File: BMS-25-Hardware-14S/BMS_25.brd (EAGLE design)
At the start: 139.7 x 52.1 mm, 218 parts, among them IC1 PBQ79656PAPTQ1, IC2 PBQ79656PAPTQ1, T1 PBHV8115X, 115, T2 PBHV8115X, 115

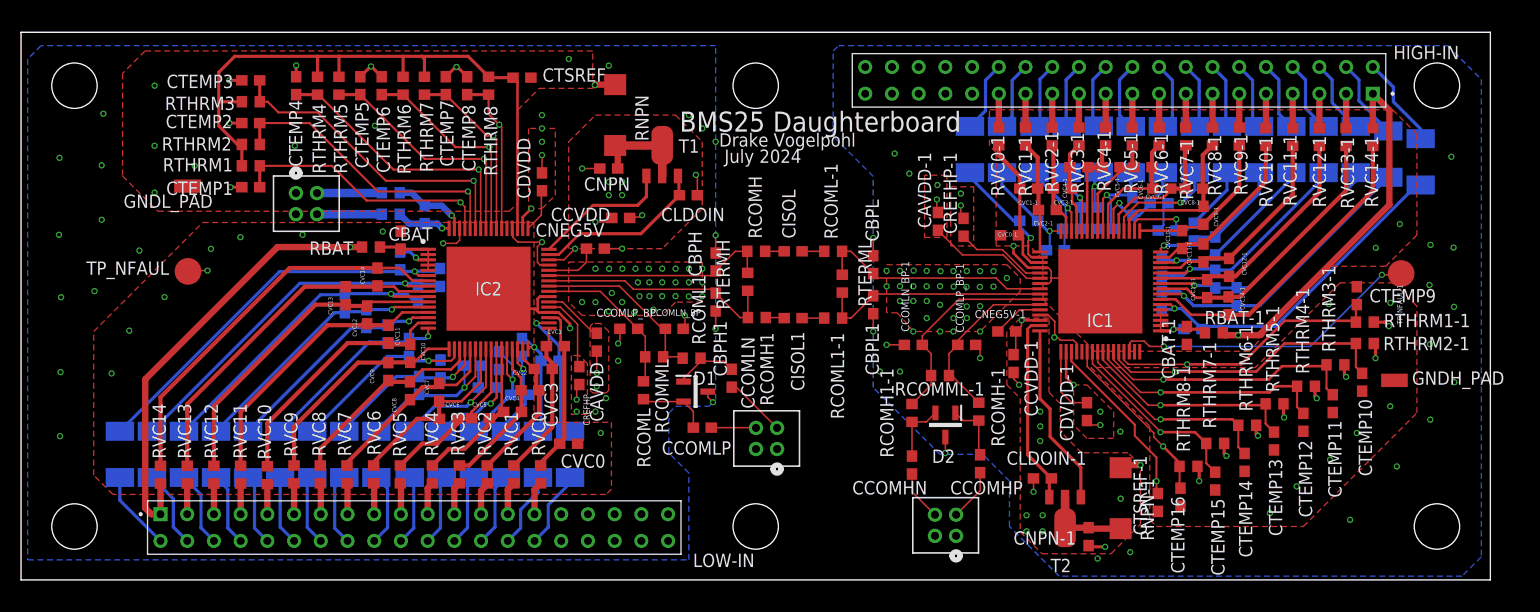
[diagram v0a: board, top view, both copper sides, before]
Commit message: Fixed Ground wiring
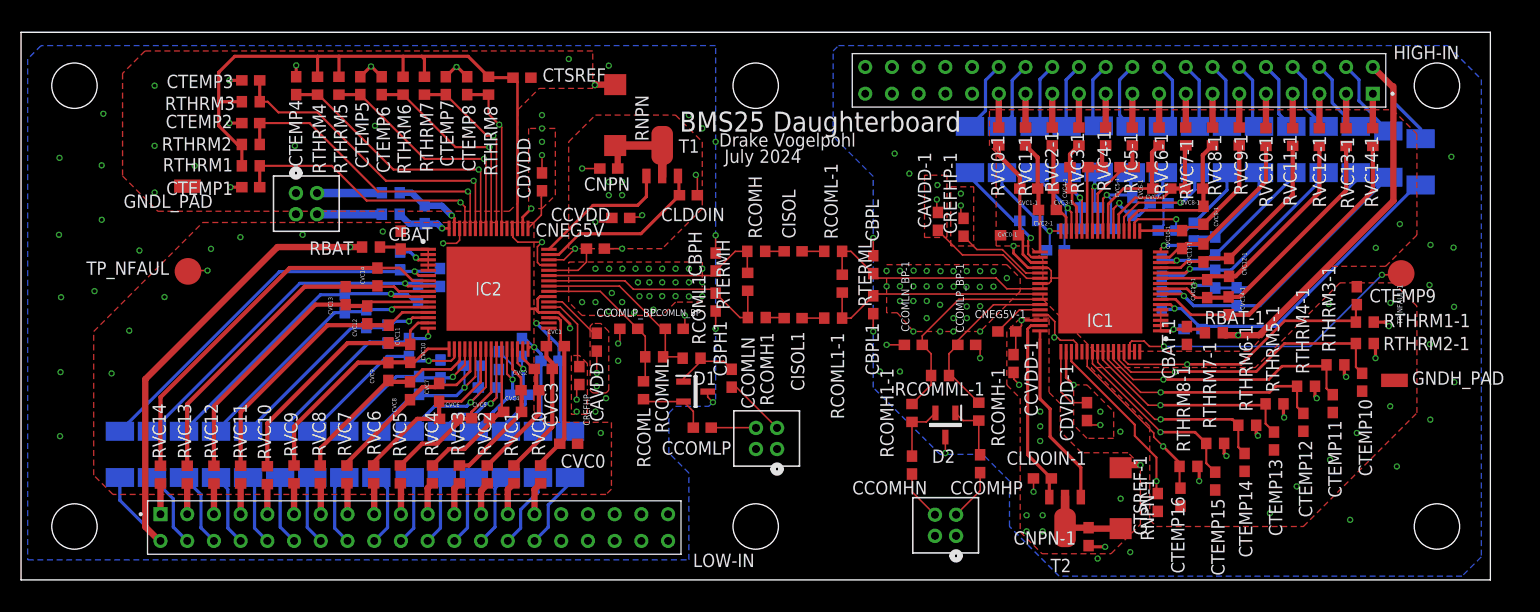
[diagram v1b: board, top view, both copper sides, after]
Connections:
- removed net CB14-IN: LOW-IN.02, RCB14.1
- removed net CB14-IN-1: HIGH-IN.02, RCB14-1.1
- new net VC14-IN: LOW-IN.01, RVC14.1
- new net VC14-IN-1: HIGH-IN.01, RVC14-1.1
- net BAT: now also LOW-IN.02, RCB14.1; no longer LOW-IN.01, RVC14.1
- net BAT-1: now also HIGH-IN.02, RCB14-1.1; no longer HIGH-IN.01, RVC14-1.1
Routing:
- net CB14-IN-1: track 8.73 -> 0.00 mm
- net BAT-1: track 55.5 -> 63.9 mm
- net CB14-IN: track 7.63 -> 0.00 mm
- net BAT: track 74.3 -> 81.1 mm
- net VC14-IN-1: track 0.00 -> 3.26 mm
- net VC14-IN: track 0.00 -> 2.91 mm

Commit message: Changed Connectors, pass DRC
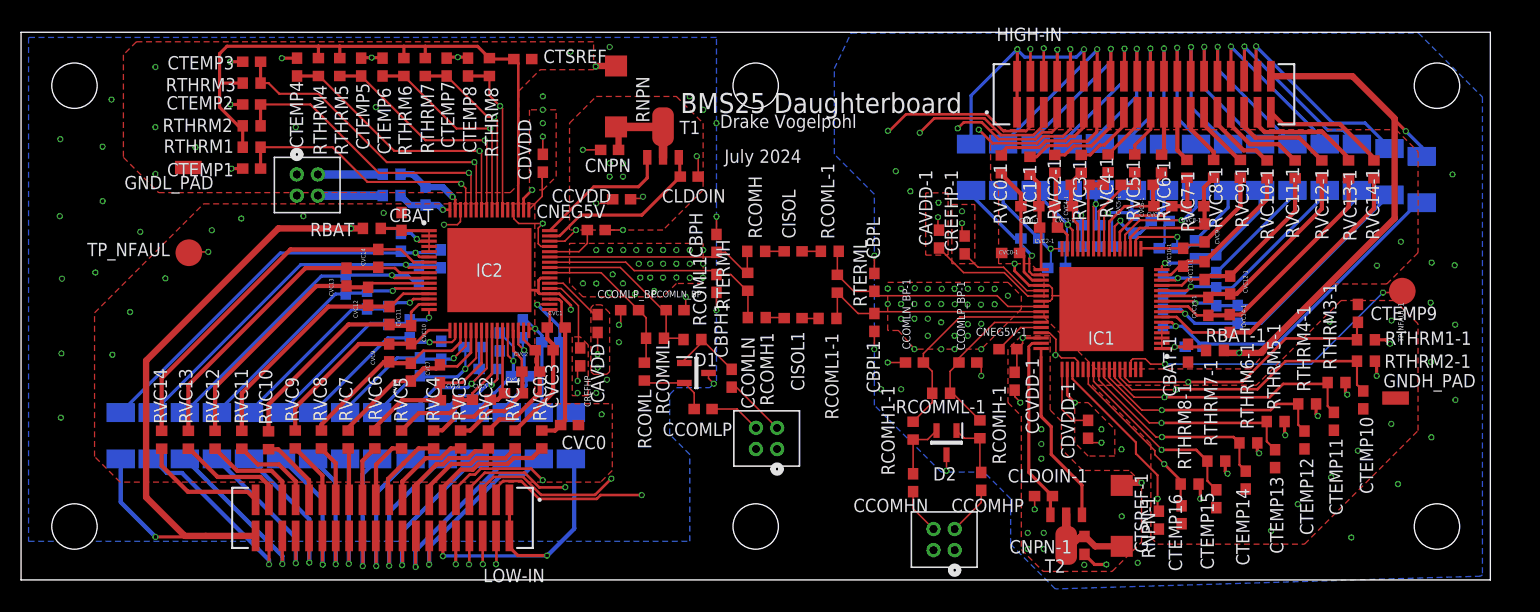
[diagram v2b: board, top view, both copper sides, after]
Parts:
- HIGH-IN, LOW-IN: value 87606-320LF -> TFM-120-02-L-D; device 87606-320LF:AMPHENOL_87606-320LF -> TFM-120-02-L-D:SAMTEC_TFM-120-02-L-D
- moved RVC10 3.32 mm to (23.5, 13.3)
- moved RVC0 3.32 mm to (49.5, 13.4)
- moved RVC1 3.32 mm to (47.0, 13.4)
- moved RVC11 3.32 mm to (21.0, 13.3)
- moved RVC12 3.32 mm to (18.5, 13.3)
- moved RVC13 3.32 mm to (15.9, 13.3)
- moved RVC14 3.32 mm to (13.4, 13.3)
- moved RVC2 3.32 mm to (44.4, 13.4)
- moved RVC3 3.32 mm to (41.8, 13.4)
- moved RVC4 3.32 mm to (39.2, 13.4)
- moved RVC5 3.32 mm to (36.2, 13.4)
- moved RVC6 3.32 mm to (33.6, 13.4)
- moved RVC7 3.32 mm to (31.1, 13.4)
- moved RVC8 3.32 mm to (28.6, 13.4)
- moved RVC9 3.32 mm to (26.1, 13.4)
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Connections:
- removed net CB0-IN: LOW-IN.30, RCB0.1
- removed net CB0-IN-1: HIGH-IN.30, RCB0-1.1
- new net VC0-IN: LOW-IN.11, RVC0.1
- new net VC0-IN-1: HIGH-IN.11, RVC0-1.1
- net BAT: now also LOW-IN.40; no longer LOW-IN.02
- net BAT-1: now also HIGH-IN.40; no longer HIGH-IN.02
- net CB1-IN: now also LOW-IN.14; no longer LOW-IN.28
- net CB1-IN-1: now also HIGH-IN.14; no longer HIGH-IN.28
- net CB10-IN: now also LOW-IN.32; no longer LOW-IN.10
- net CB10-IN-1: now also HIGH-IN.32; no longer HIGH-IN.10
- net CB11-IN: now also LOW-IN.34; no longer LOW-IN.08
- net CB11-IN-1: now also HIGH-IN.34; no longer HIGH-IN.08
- net CB12-IN: now also LOW-IN.36; no longer LOW-IN.06
- net CB12-IN-1: now also HIGH-IN.36; no longer HIGH-IN.06
- net CB13-IN: now also LOW-IN.38; no longer LOW-IN.04
- net CB13-IN-1: now also HIGH-IN.38; no longer HIGH-IN.04
- net CB2-IN: now also LOW-IN.16; no longer LOW-IN.26
- net CB2-IN-1: now also HIGH-IN.16; no longer HIGH-IN.26
- net CB3-IN: now also LOW-IN.18; no longer LOW-IN.24
- net CB3-IN-1: now also HIGH-IN.18; no longer HIGH-IN.24
- net CB4-IN: now also LOW-IN.20; no longer LOW-IN.22
- net CB4-IN-1: now also HIGH-IN.20; no longer HIGH-IN.22
- net CB5-IN: now also LOW-IN.22; no longer LOW-IN.20
- net CB5-IN-1: now also HIGH-IN.22; no longer HIGH-IN.20
- net CB6-IN: now also LOW-IN.24; no longer LOW-IN.18
- net CB6-IN-1: now also HIGH-IN.24; no longer HIGH-IN.18
- net CB7-IN: now also LOW-IN.26; no longer LOW-IN.16
- net CB7-IN-1: now also HIGH-IN.26; no longer HIGH-IN.16
- net CB8-IN: now also LOW-IN.28; no longer LOW-IN.14
- net CB8-IN-1: now also HIGH-IN.28; no longer HIGH-IN.14
- net CB9-IN: now also LOW-IN.30; no longer LOW-IN.12
- net CB9-IN-1: now also HIGH-IN.30; no longer HIGH-IN.12
- net GNDH: now also HIGH-IN.01, HIGH-IN.02, HIGH-IN.12, RCB0-1.1; no longer HIGH-IN.29, HIGH-IN.39, HIGH-IN.40, RVC0-1.1
- net GNDL: now also LOW-IN.01, LOW-IN.02, LOW-IN.12, RCB0.1; no longer LOW-IN.29, LOW-IN.39, LOW-IN.40, RVC0.1
- net TEMP1: now also LOW-IN.09; no longer LOW-IN.31
- net TEMP10: now also HIGH-IN.10; no longer HIGH-IN.32
- net TEMP11: now also HIGH-IN.07; no longer HIGH-IN.33
- net TEMP12: now also HIGH-IN.08; no longer HIGH-IN.34
- net TEMP13: now also HIGH-IN.05; no longer HIGH-IN.35
- net TEMP14: now also HIGH-IN.06; no longer HIGH-IN.36
- net TEMP15: now also HIGH-IN.03; no longer HIGH-IN.37
- net TEMP16: now also HIGH-IN.04; no longer HIGH-IN.38
- net TEMP2: now also LOW-IN.10; no longer LOW-IN.32
- net TEMP3: now also LOW-IN.07; no longer LOW-IN.33
- net TEMP4: now also LOW-IN.08; no longer LOW-IN.34
- net TEMP5: now also LOW-IN.05; no longer LOW-IN.35
- net TEMP6: now also LOW-IN.06; no longer LOW-IN.36
- net TEMP7: now also LOW-IN.03; no longer LOW-IN.37
- net TEMP8: now also LOW-IN.04; no longer LOW-IN.38
- net TEMP9: now also HIGH-IN.09; no longer HIGH-IN.31
- net VC1-IN: now also LOW-IN.13; no longer LOW-IN.27
- net VC1-IN-1: now also HIGH-IN.13; no longer HIGH-IN.27
- net VC10-IN: now also LOW-IN.31; no longer LOW-IN.09
- net VC10-IN-1: now also HIGH-IN.31; no longer HIGH-IN.09
- net VC11-IN: now also LOW-IN.33; no longer LOW-IN.07
- net VC11-IN-1: now also HIGH-IN.33; no longer HIGH-IN.07
- net VC12-IN: now also LOW-IN.35; no longer LOW-IN.05
- net VC12-IN-1: now also HIGH-IN.35; no longer HIGH-IN.05
- net VC13-IN: now also LOW-IN.37; no longer LOW-IN.03
- net VC13-IN-1: now also HIGH-IN.37; no longer HIGH-IN.03
- net VC14-IN: now also LOW-IN.39; no longer LOW-IN.01
- net VC14-IN-1: now also HIGH-IN.39; no longer HIGH-IN.01
- net VC2-IN: now also LOW-IN.15; no longer LOW-IN.25
- net VC2-IN-1: now also HIGH-IN.15; no longer HIGH-IN.25
- net VC3-IN: now also LOW-IN.17; no longer LOW-IN.23
- net VC3-IN-1: now also HIGH-IN.17; no longer HIGH-IN.23
- net VC4-IN: now also LOW-IN.19; no longer LOW-IN.21
- net VC4-IN-1: now also HIGH-IN.19; no longer HIGH-IN.21
- net VC5-IN: now also LOW-IN.21; no longer LOW-IN.19
- net VC5-IN-1: now also HIGH-IN.21; no longer HIGH-IN.19
- net VC6-IN: now also LOW-IN.23; no longer LOW-IN.17
- net VC6-IN-1: now also HIGH-IN.23; no longer HIGH-IN.17
- net VC7-IN: now also LOW-IN.25; no longer LOW-IN.15
- net VC7-IN-1: now also HIGH-IN.25; no longer HIGH-IN.15
- net VC8-IN: now also LOW-IN.27; no longer LOW-IN.13
- net VC8-IN-1: now also HIGH-IN.27; no longer HIGH-IN.13
- net VC9-IN: now also LOW-IN.29; no longer LOW-IN.11
- net VC9-IN-1: now also HIGH-IN.29; no longer HIGH-IN.11
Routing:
- net GNDL: track 49.7 -> 76.2 mm, vias 90 -> 92
- net GNDH: track 39.3 -> 63.3 mm, vias 82 -> 84
- net TEMP8: track 61.4 -> 79.7 mm, vias 1 -> 2
- net TEMP6: track 63.5 -> 81.1 mm, vias 1 -> 2
- net TEMP7: track 58.9 -> 75.0 mm, vias 1 -> 2
- net BAT: track 81.1 -> 95.9 mm, vias 2 -> 3
- net TEMP4: track 66.6 -> 80.8 mm, vias 1 -> 2
- net TEMP16: track 67.3 -> 81.4 mm, vias 1 -> 2
- net TEMP5: track 61.9 -> 75.3 mm, vias 1 -> 2
- net TEMP15: track 65.0 -> 77.3 mm, vias 1 -> 2
- net VC0-IN: track 0.00 -> 12.2 mm
- net CB13-IN-1: track 7.74 -> 19.7 mm, vias 0 -> 1
- net CB1-IN: track 7.22 -> 18.3 mm, vias 0 -> 1
- net CB13-IN: track 7.42 -> 18.2 mm, vias 0 -> 1
- net VC0-IN-1: track 0.00 -> 10.5 mm
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
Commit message: Updated Change to daughteboard 14s for final manufacturing
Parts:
- removed CCOMHN, CCOMHP, CCOMLN, CCOMLP, CISOL, CISOL1: 2.2nF, NFR23_v1.3:C0603
- removed HIGH-IN, LOW-IN: TFM-120-02-L-D, TFM-120-02-L-D:SAMTEC_TFM-120-02-L-D
- removed RNPN, RNPN-1: 150?, rcl:R2512W
- added C1, C2, C3, C4, C5, C6: C1206C105K5RACTU, C1206C105K5RACTU:CAPC3216X120N
- added J1, J2: TFM-120-02-L-D-A, TFM-120-02-L-D-A:TFM-120-ZZ-XXX-D-A
- added R1, R4: RC2512JK-07560RL, RC2512JK-07560RL:RESC6331X65N
- added RGNDH, RGNDL: 0, NFR23_v1.3:R0603
- added TP1, TP2, TP3, TP4: 5002, 5002:KEYSTONE_5002
- RCB0, RCB0-1, RCB1, RCB1-1, RCB10, RCB10-1, RCB11, RCB11-1, RCB12, RCB12-1, RCB13, RCB13-1, RCB14, RCB14-1, RCB2, RCB2-1, RCB3, RCB3-1, RCB4, RCB4-1, RCB5, RCB5-1, RCB6, RCB6-1, RCB7, RCB7-1, RCB8, RCB8-1, RCB9, RCB9-1: value 10 -> 50
- moved RCOML1-1 0.84 mm to (77.5, 24.9)
- moved RCOML-1 0.39 mm to (77.3, 31.2)
- moved RCOMH 0.38 mm to (69.5, 31.2)
- moved RCOMH1 0.23 mm to (69.7, 24.9)
- moved RCB7 0.06 mm to (30.9, 13.7)
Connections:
- new net CB0-IN: RCB0.1, RGNDL.2
- new net CB0-IN-1: RCB0-1.1, RGNDH.2
- net BAT: now also J1.40, R1.1; no longer LOW-IN.40, RNPN.1
- net BAT-1: now also J2.40, R4.1; no longer HIGH-IN.40, RNPN-1.1
- net CB1-IN: now also J1.14; no longer LOW-IN.14
- net CB1-IN-1: now also J2.14; no longer HIGH-IN.14
- net CB10-IN: now also J1.32; no longer LOW-IN.32
- net CB10-IN-1: now also J2.32; no longer HIGH-IN.32
- net CB11-IN: now also J1.34; no longer LOW-IN.34
- net CB11-IN-1: now also J2.34; no longer HIGH-IN.34
- net CB12-IN: now also J1.36; no longer LOW-IN.36
- net CB12-IN-1: now also J2.36; no longer HIGH-IN.36
- net CB13-IN: now also J1.38; no longer LOW-IN.38
- net CB13-IN-1: now also J2.38; no longer HIGH-IN.38
- net CB2-IN: now also J1.16; no longer LOW-IN.16
- net CB2-IN-1: now also J2.16; no longer HIGH-IN.16
- net CB3-IN: now also J1.18; no longer LOW-IN.18
- net CB3-IN-1: now also J2.18; no longer HIGH-IN.18
- net CB4-IN: now also J1.20; no longer LOW-IN.20
- net CB4-IN-1: now also J2.20; no longer HIGH-IN.20
- net CB5-IN: now also J1.22; no longer LOW-IN.22
- net CB5-IN-1: now also J2.22; no longer HIGH-IN.22
- net CB6-IN: now also J1.24; no longer LOW-IN.24
- net CB6-IN-1: now also J2.24; no longer HIGH-IN.24
- net CB7-IN: now also J1.26; no longer LOW-IN.26
- net CB7-IN-1: now also J2.26; no longer HIGH-IN.26
- net CB8-IN: now also J1.28; no longer LOW-IN.28
- net CB8-IN-1: now also J2.28; no longer HIGH-IN.28
- net CB9-IN: now also J1.30; no longer LOW-IN.30
- net CB9-IN-1: now also J2.30; no longer HIGH-IN.30
- net GNDH: now also J2.1, J2.12, J2.2, RGNDH.1, TP3.TP; no longer HIGH-IN.01, HIGH-IN.02, HIGH-IN.12, RCB0-1.1
- net GNDL: now also J1.1, J1.12, J1.2, RGNDL.1, TP4.TP; no longer LOW-IN.01, LOW-IN.02, LOW-IN.12, RCB0.1
- net ISO_COMN: now also C2.2; no longer CISOL1.1
- net ISO_COMP: now also C1.2; no longer CISOL.1
- net N$101: now also C5.2; no longer CCOMHN.1
- net N$103: now also C3.1; no longer CCOMLN.1
- net N$104: now also C4.1; no longer CCOMLP.1
- net N$2: now also R1.2; no longer RNPN.2
- net N$46: now also C1.1; no longer CISOL.2
- net N$47: now also C2.1; no longer CISOL1.2
- net N$50: now also C3.2; no longer CCOMLN.2
- net N$51: now also C4.2; no longer CCOMLP.2
- net N$92: now also R4.2; no longer RNPN-1.2
- net N$97: now also C6.1; no longer CCOMHP.2
- net N$98: now also C5.1; no longer CCOMHN.2
- net N$99: now also C6.2; no longer CCOMHP.1
- net TEMP1: now also J1.9; no longer LOW-IN.09
- net TEMP10: now also J2.10; no longer HIGH-IN.10
- net TEMP11: now also J2.7; no longer HIGH-IN.07
- net TEMP12: now also J2.8; no longer HIGH-IN.08
- net TEMP13: now also J2.5; no longer HIGH-IN.05
- net TEMP14: now also J2.6; no longer HIGH-IN.06
- net TEMP15: now also J2.3; no longer HIGH-IN.03
- net TEMP16: now also J2.4; no longer HIGH-IN.04
- net TEMP2: now also J1.10; no longer LOW-IN.10
- net TEMP3: now also J1.7; no longer LOW-IN.07
- net TEMP4: now also J1.8; no longer LOW-IN.08
- net TEMP5: now also J1.5; no longer LOW-IN.05
- net TEMP6: now also J1.6; no longer LOW-IN.06
- net TEMP7: now also J1.3; no longer LOW-IN.03
- net TEMP8: now also J1.4; no longer LOW-IN.04
- net TEMP9: now also J2.9; no longer HIGH-IN.09
- net TP: now also TP2.TP
- net TP-1: now also TP1.TP
- net VC0-IN: now also J1.11; no longer LOW-IN.11
- net VC0-IN-1: now also J2.11; no longer HIGH-IN.11
- net VC1-IN: now also J1.13; no longer LOW-IN.13
- net VC1-IN-1: now also J2.13; no longer HIGH-IN.13
- net VC10-IN: now also J1.31; no longer LOW-IN.31
- net VC10-IN-1: now also J2.31; no longer HIGH-IN.31
- net VC11-IN: now also J1.33; no longer LOW-IN.33
- net VC11-IN-1: now also J2.33; no longer HIGH-IN.33
- net VC12-IN: now also J1.35; no longer LOW-IN.35
- net VC12-IN-1: now also J2.35; no longer HIGH-IN.35
- net VC13-IN: now also J1.37; no longer LOW-IN.37
- net VC13-IN-1: now also J2.37; no longer HIGH-IN.37
- net VC14-IN: now also J1.39; no longer LOW-IN.39
- net VC14-IN-1: now also J2.39; no longer HIGH-IN.39
- net VC2-IN: now also J1.15; no longer LOW-IN.15
- net VC2-IN-1: now also J2.15; no longer HIGH-IN.15
- net VC3-IN: now also J1.17; no longer LOW-IN.17
- net VC3-IN-1: now also J2.17; no longer HIGH-IN.17
- net VC4-IN: now also J1.19; no longer LOW-IN.19
- net VC4-IN-1: now also J2.19; no longer HIGH-IN.19
- net VC5-IN: now also J1.21; no longer LOW-IN.21
- net VC5-IN-1: now also J2.21; no longer HIGH-IN.21
- net VC6-IN: now also J1.23; no longer LOW-IN.23
- net VC6-IN-1: now also J2.23; no longer HIGH-IN.23
- net VC7-IN: now also J1.25; no longer LOW-IN.25
- net VC7-IN-1: now also J2.25; no longer HIGH-IN.25
- net VC8-IN: now also J1.27; no longer LOW-IN.27
- net VC8-IN-1: now also J2.27; no longer HIGH-IN.27
- net VC9-IN: now also J1.29; no longer LOW-IN.29
- net VC9-IN-1: now also J2.29; no longer HIGH-IN.29
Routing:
- net BAT-1: track 69.2 -> 85.7 mm
- net GNDL: track 76.2 -> 62.0 mm, vias 92 -> 97
- net GNDH: track 63.3 -> 57.0 mm, vias 84 -> 94
- net BAT: track 95.9 -> 101.6 mm
- net CB0-IN: track 0.00 -> 5.27 mm
- net CB0-IN-1: track 0.00 -> 4.21 mm
- net TP-1: track 29.8 -> 32.9 mm
- net TP: track 28.2 -> 31.1 mm
- net VC5-IN-1: track 4.66 -> 7.18 mm
- net N$2: track 9.10 -> 11.2 mm
- net N$50: track 6.81 -> 8.62 mm
- net TEMP1: track 68.4 -> 66.9 mm
- net TEMP3: track 76.0 -> 74.5 mm
- net TEMP7: track 75.0 -> 73.7 mm
- net N$99: track 4.73 -> 3.51 mm
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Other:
- board text added: "Janurary 2025"
- board text removed: "July 2024"

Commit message: Daughterboard Updated
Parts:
- moved CNPN-1 0.84 mm to (101.9, 3.20)
- moved R4 0.69 mm to (104.9, 6.17)
- moved T2 0.53 mm to (98.8, 4.21)
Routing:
- net GNDH: track 57.0 -> 56.1 mm
- net N$92: track 8.02 -> 8.88 mm
- net BAT-1: track 85.7 -> 85.0 mm
